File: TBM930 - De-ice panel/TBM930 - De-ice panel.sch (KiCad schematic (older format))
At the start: 68 parts, among them J1 SW_AIRFRAME_DE_ICE, J10 AVR-ISP-6, J2 SW_ICE_LIGHT, J3 SW_PROP_DE_ICE, J4 SW_WIND_SHIELD, J5 SW_PITOT_L_HTR, J6 SW_PITOT_R_HTR, J7 SW_INERT_SEP, J8 Barrel_Jack, J9 USB_B_Micro, SW1 SW_Push, SW2 SW_Push, U1 TLC5917IN, U2 TLC5917IN, U3 ATmega32U4-MU, Y1 Crystal_GND24

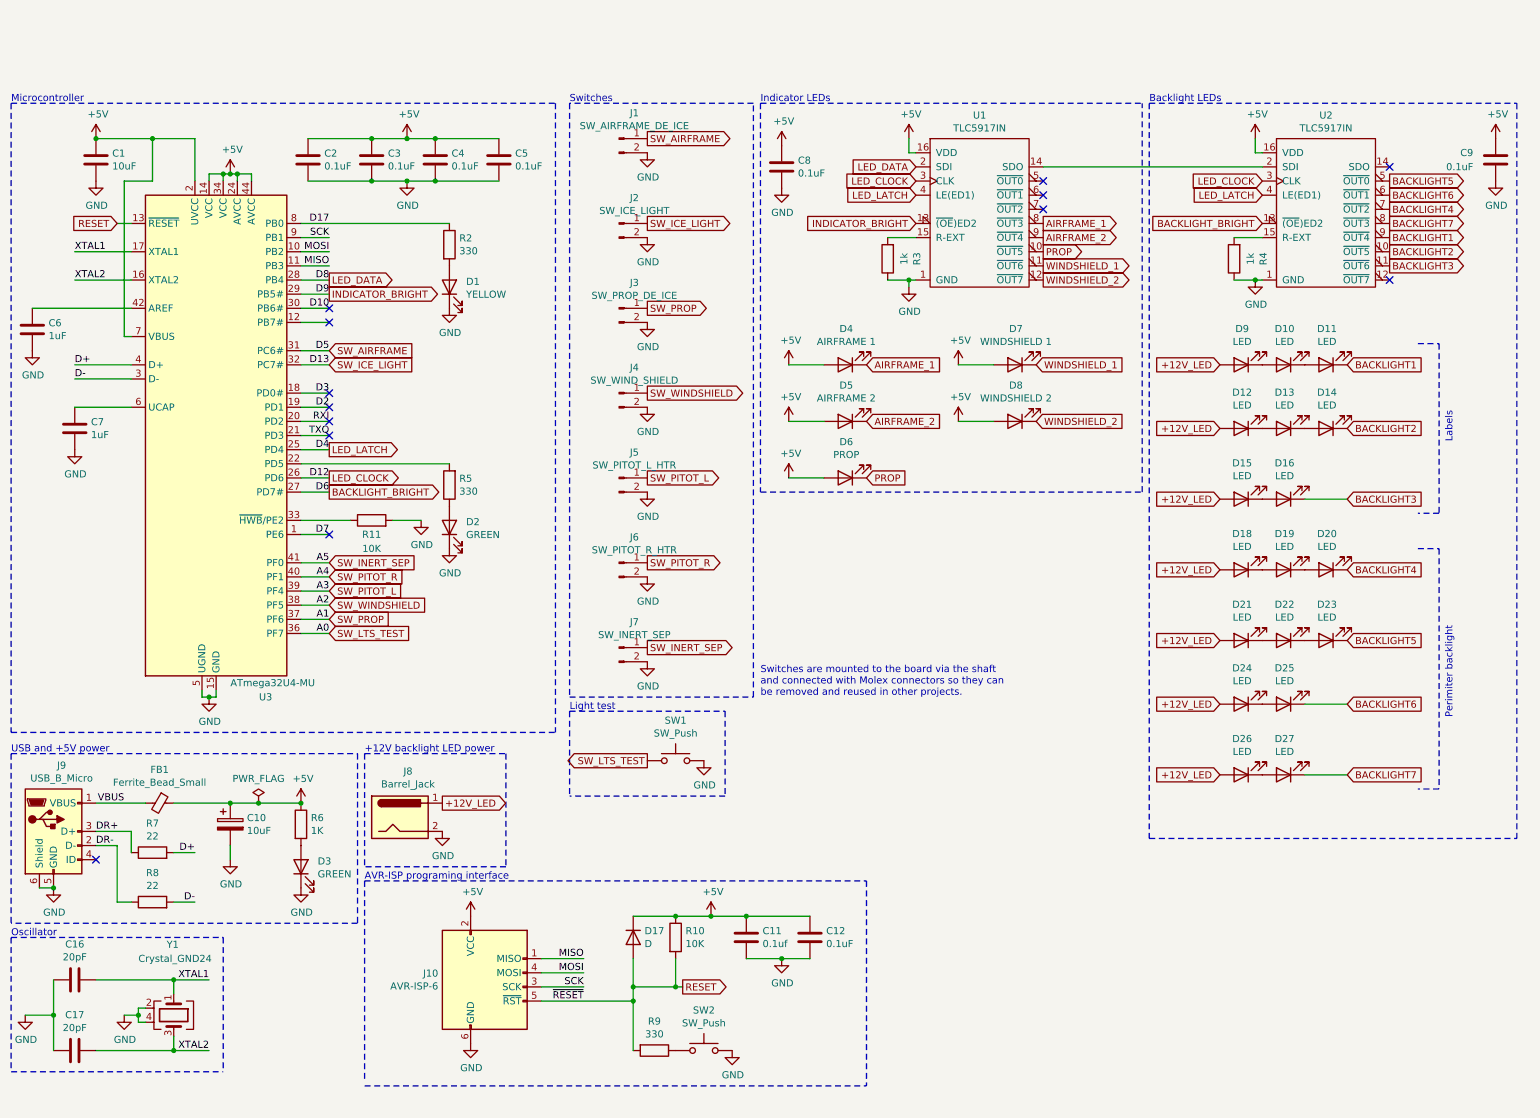
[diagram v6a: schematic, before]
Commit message: Massive PCB reroute
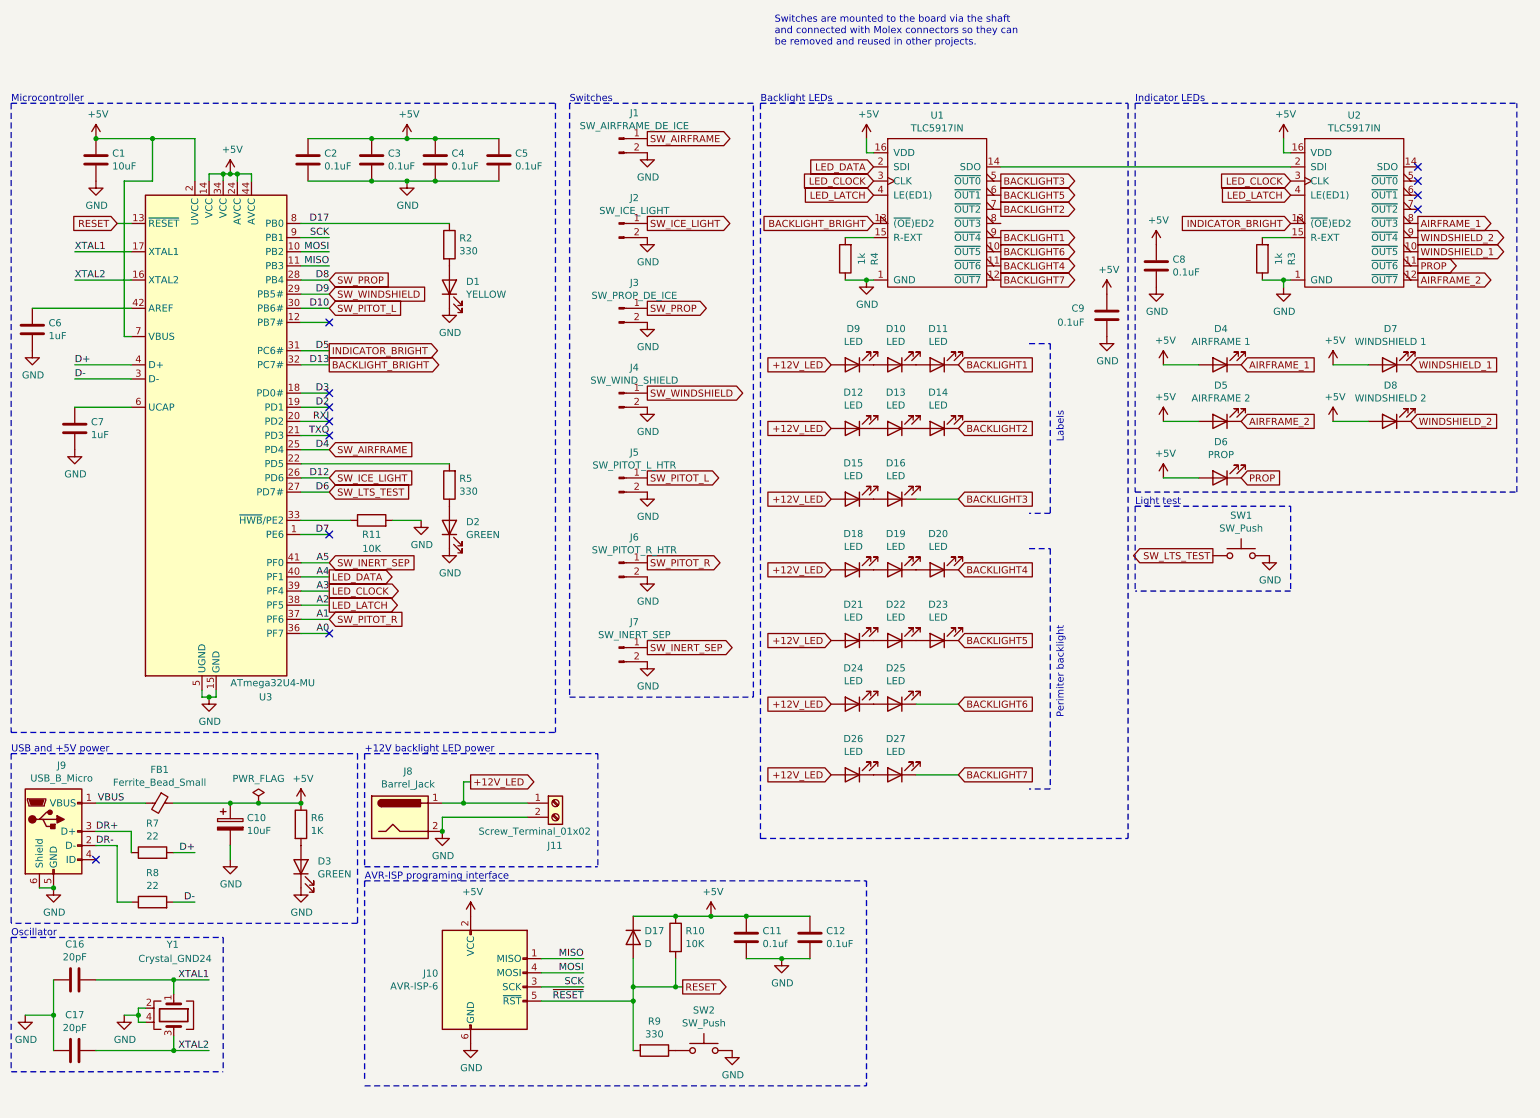
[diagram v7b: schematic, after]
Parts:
- added J11: Screw_Terminal_01x02, TerminalBlock_Philmore:TerminalBlock_Philmore_TB132_1x02_P5.00mm_Horizontal, symbol Connector:Screw_Terminal_01x02
- renumbered U2 to U1, U1 to U2
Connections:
- net D10 is gone; now on net SW_PITOT_L: U3.30 (PB6#)
- net +12V_LED: now also J11.1 (Pin_1)
- net AIRFRAME_2: now also U2.12 (~OUT7); no longer U2.9 (~OUT4)
- net BACKLIGHT2: now also U1.7 (~OUT2); no longer U1.10 (~OUT5)
- net BACKLIGHT3: now also U1.5 (~OUT0); no longer U1.11 (~OUT6)
- net BACKLIGHT4: now also U1.11 (~OUT6); no longer U1.7 (~OUT2)
- net BACKLIGHT5: now also U1.6 (~OUT1); no longer U1.5 (~OUT0)
- net BACKLIGHT6: now also U1.10 (~OUT5); no longer U1.6 (~OUT1)
- net BACKLIGHT7: now also U1.12 (~OUT7); no longer U1.8 (~OUT3)
- net BACKLIGHT_BRIGHT: now also U3.32 (PC7#); no longer U3.27 (PD7#)
- net GND: now also J11.2 (Pin_2)
- net INDICATOR_BRIGHT: now also U3.31 (PC6#); no longer U3.29 (PB5#)
- net LED_CLOCK: now also U3.39 (PF4); no longer U3.26 (PD6)
- net LED_DATA: now also U1.2 (SDI), U3.40 (PF1); no longer U2.2 (SDI), U3.28 (PB4)
- net LED_LATCH: now also U3.38 (PF5); no longer U3.25 (PD4)
- net PROP: now also U2.11 (~OUT6); no longer U2.10 (~OUT5)
- net SW_AIRFRAME: now also U3.25 (PD4); no longer U3.31 (PC6#)
- net SW_ICE_LIGHT: now also U3.26 (PD6); no longer U3.32 (PC7#)
- net SW_LTS_TEST: now also U3.27 (PD7#); no longer U3.36 (PF7)
- net SW_PITOT_L: no longer U3.39 (PF4)
- net SW_PITOT_R: now also U3.37 (PF6); no longer U3.40 (PF1)
- net SW_PROP: now also U3.28 (PB4); no longer U3.37 (PF6)
- net SW_WINDSHIELD: now also U3.29 (PB5#); no longer U3.38 (PF5)
- net WINDSHIELD_1: now also U2.10 (~OUT5); no longer U2.11 (~OUT6)
- net WINDSHIELD_2: now also U2.9 (~OUT4); no longer U2.12 (~OUT7)
- net at U2.14 (SDO): no longer U1.2 (SDI)
- net at U1.14 (SDO): now also U2.2 (SDI)
- new net A0: U3.36 (PF7)
- no-connect marks 13 -> 12
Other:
- moved on the sheet: C8, C9, D10, D11, D12, D13, D14, D15, D16, D18, D19, D20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

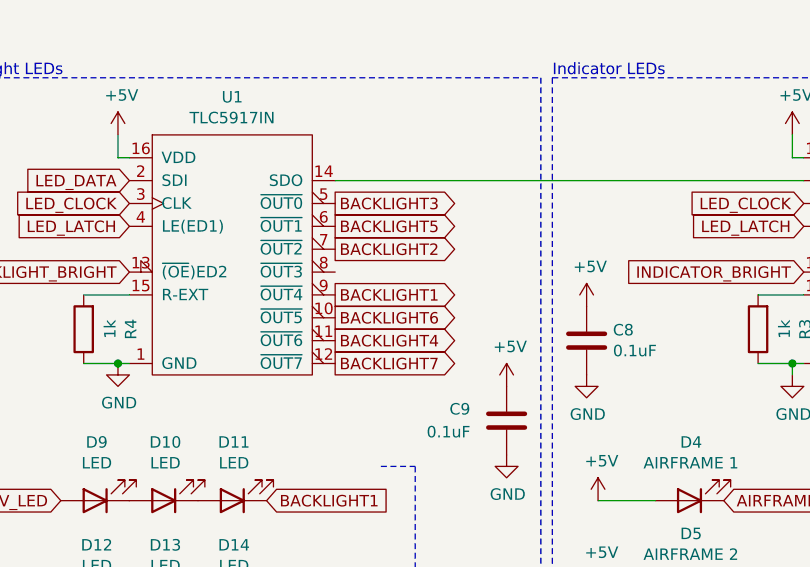
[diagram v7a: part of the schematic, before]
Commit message: Fully routed v2
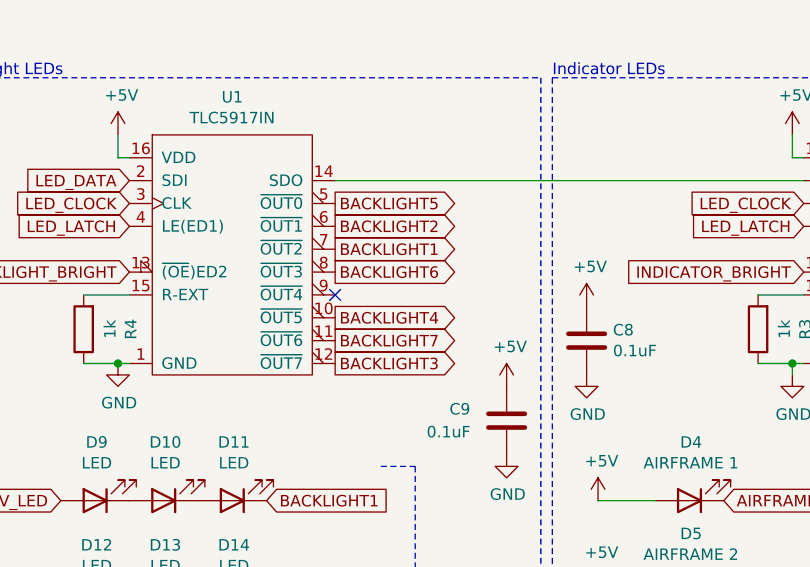
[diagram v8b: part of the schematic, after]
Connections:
- net BACKLIGHT1: now also U1.7 (~OUT2); no longer U1.9 (~OUT4)
- net BACKLIGHT2: now also U1.6 (~OUT1); no longer U1.7 (~OUT2)
- net BACKLIGHT3: now also U1.12 (~OUT7); no longer U1.5 (~OUT0)
- net BACKLIGHT4: now also U1.10 (~OUT5); no longer U1.11 (~OUT6)
- net BACKLIGHT5: now also U1.5 (~OUT0); no longer U1.6 (~OUT1)
- net BACKLIGHT6: now also U1.8 (~OUT3); no longer U1.10 (~OUT5)
- net BACKLIGHT7: now also U1.11 (~OUT6); no longer U1.12 (~OUT7)
- no-connect marks 12 -> 13
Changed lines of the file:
@@
 Text GLabel 7200 4400 2    50   Input ~ 0
 BACKLIGHT5
-Text GLabel 7500 1750 2    50   Output ~ 0
+Text GLabel 7500 1650 2    50   Output ~ 0
 BACKLIGHT4
-Text GLabel 7500 1250 2    50   Output ~ 0
+Text GLabel 7500 1150 2    50   Output ~ 0
 BACKLIGHT5
 $Comp
@@
 Text GLabel 6600 1250 0    50   Input ~ 0
 LED_LATCH
-Text GLabel 7500 1150 2    50   Output ~ 0
+Text GLabel 7500 1850 2    50   Output ~ 0
 BACKLIGHT3
+Text GLabel 7500 1250 2    50   Output ~ 0
+BACKLIGHT2
 Text GLabel 7500 1350 2    50   Output ~ 0
-BACKLIGHT2
-Text GLabel 7500 1550 2    50   Output ~ 0
 BACKLIGHT1
 Wire Notes Line
@@
 Text GLabel 7200 4850 2    50   Input ~ 0
 BACKLIGHT6
-Text GLabel 7500 1650 2    50   Output ~ 0
+Text GLabel 7500 1450 2    50   Output ~ 0
 BACKLIGHT6
 $Comp
@@
 	-1   0    0    1
 $EndComp
-Text GLabel 7500 1850 2    50   Output ~ 0
+Text GLabel 7500 1750 2    50   Output ~ 0
 BACKLIGHT7
 Wire Wire Line
@@
 SW_AIRFRAME
 NoConn ~ 2750 4350
+NoConn ~ 7500 1550
 $EndSCHEMATC
